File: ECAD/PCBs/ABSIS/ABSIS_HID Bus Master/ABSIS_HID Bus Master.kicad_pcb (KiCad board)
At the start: 2 copper layers, 90.8 x 53.3 mm, 19 parts, among them J1 PWR IN, J2 BUS #1, U0 ProMicro, U1 MAX487EESA+T

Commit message: Drawing Sheet & Silkscreen Update - ABSIS
On all ABSIS PCBs:

1:  Updated/Relinked Drawing Sheet for both PCB and Schematics
2:  Standardized Silkscreen (if required)
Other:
- board text added: "REV: 2"
- board text removed: "REV: 1"
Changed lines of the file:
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@@
   (paper "A4")
   (title_block
-    (title "ABSIS RS485 BUS MASTER")
-    (date "2020-11-04")
+    (title "ABSIS HID Bus Master")
+    (date "2023-02-10")
     (rev "2")
-    (company "OPENHORNET.COM")
-    (comment 1 "CC BY-NC-SA")
+    (company "www.openhornet.com")
+    (comment 1 "License:  CC BY-NC-SA")
   )
   (layers
@@
     (effects (font (size 1 1) (thickness 0.15)))
   )
-  (gr_text "REV: 1" (at 191.643 75.819) (layer "F.SilkS")
+  (gr_text "REV: 2" (at 191.643 75.819) (layer "F.SilkS")
     (effects (font (size 0.8 0.8) (thickness 0.15)))
   )

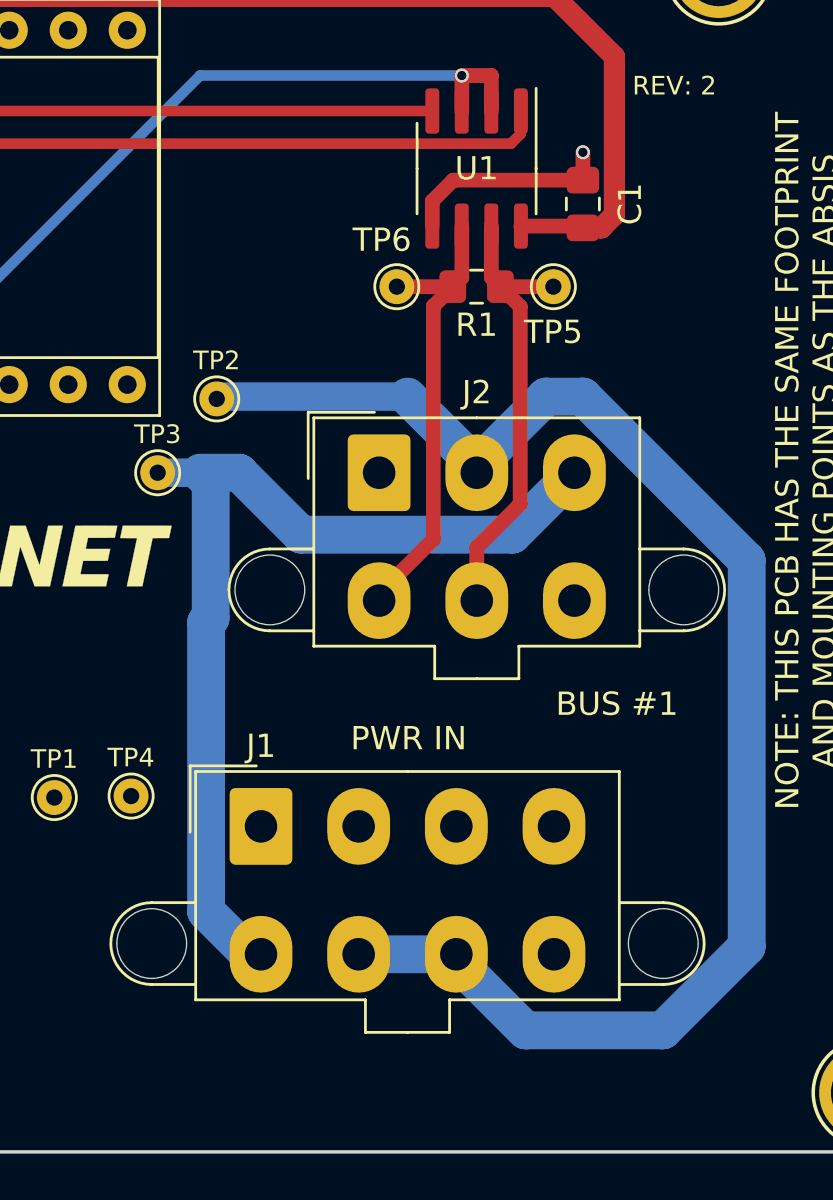
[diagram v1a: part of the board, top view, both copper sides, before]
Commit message: Review: ABSIS_HID Bus Master 100% Complete.
Updated Model and Footprint libraries
Updated PCB with correct footprint paths to point towards OH libraries
Updated production files
Added .PNGs and updated STEP file
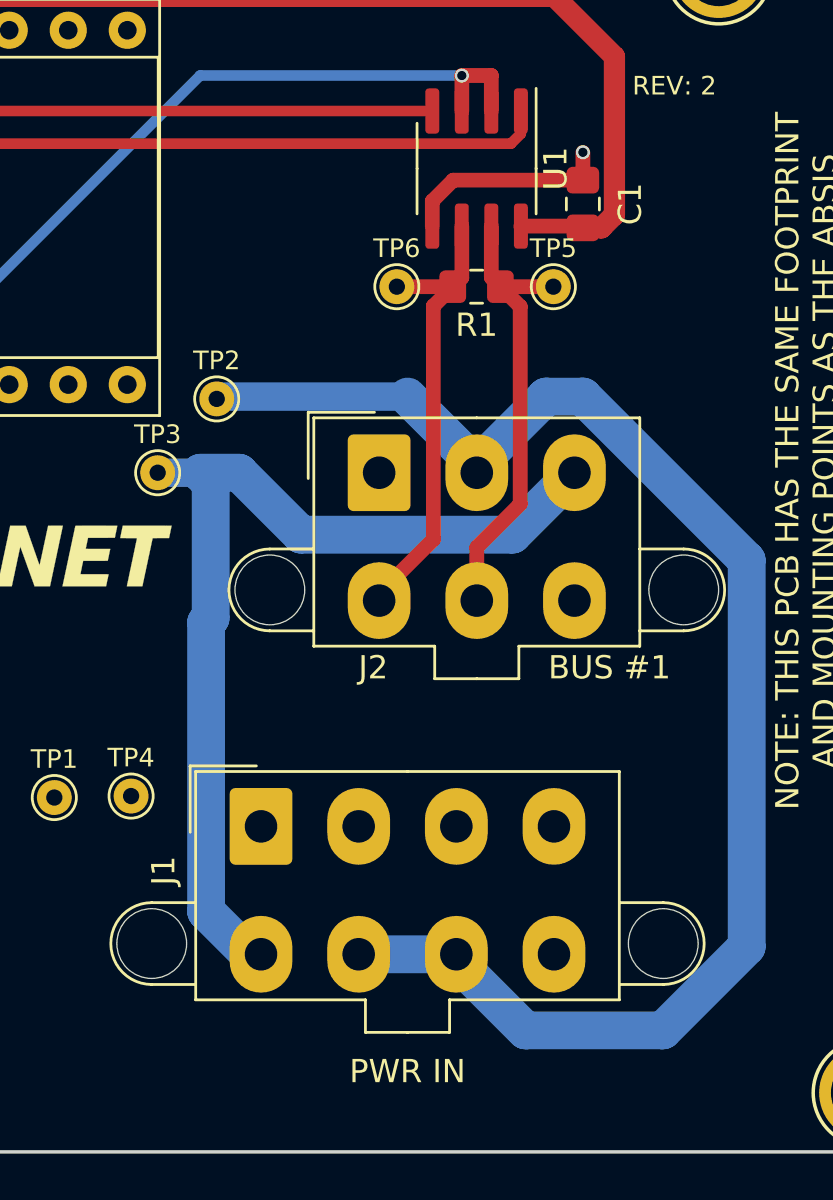
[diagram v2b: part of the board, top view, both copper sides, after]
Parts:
- C1: footprint Capacitor_SMD:C_0805_2012Metric_Pad1.15x1.40mm_HandSolder -> OH_Footprints:C_0805_2012Metric_Pad1.15x1.40mm_HandSolder
- J1: footprint Connector_Molex:Molex_Mini-Fit_Jr_5566-08A2_2x04_P4.20mm_Vertical -> OH_Footprints:Molex_Mini-Fit_Jr_5566-08A2_2x04_P4.20mm_Vertical
- J2: footprint Connector_Molex:Molex_Mini-Fit_Jr_5566-06A2_2x03_P4.20mm_Vertical -> OH_Footprints:Molex_Mini-Fit_Jr_5566-06A2_2x03_P4.20mm_Vertical
- LOGO1: footprint KiCAD Libraries:OH_LOGO_37.7mm_5.9mm -> OH_Footprints:OH_LOGO_37.7mm_5.9mm
- LOGO3: footprint KiCAD Libraries:CC-BY-NC-SA-Small -> OH_Footprints:CC-BY-NC-SA-Small
- LOGO4: footprint KiCAD Libraries:OH_LOGO_LARGE -> OH_Footprints:OH_LOGO_LARGE
- MK1, MK3, MK4, MK6: footprint Socket_Arduino_Mega:Arduino_1pin -> OH_Footprints:Arduino_1pin
- R1: footprint Resistor_SMD:R_0805_2012Metric_Pad1.15x1.40mm_HandSolder -> OH_Footprints:R_0805_2012Metric_Pad1.15x1.40mm_HandSolder
- TP1, TP2, TP3, TP4, TP5, TP6: footprint TestPoint:TestPoint_THTPad_D1.5mm_Drill0.7mm -> OH_Footprints:TestPoint_THTPad_D1.5mm_Drill0.7mm
- U0: footprint Package_DIP:DIP-24_W15.24mm_Socket -> OH_Footprints:DIP-24_W15.24mm_Socket
- U1: footprint Package_SO:SOIC-8_3.9x4.9mm_P1.27mm -> OH_Footprints:SOIC-8_3.9x4.9mm_P1.27mm

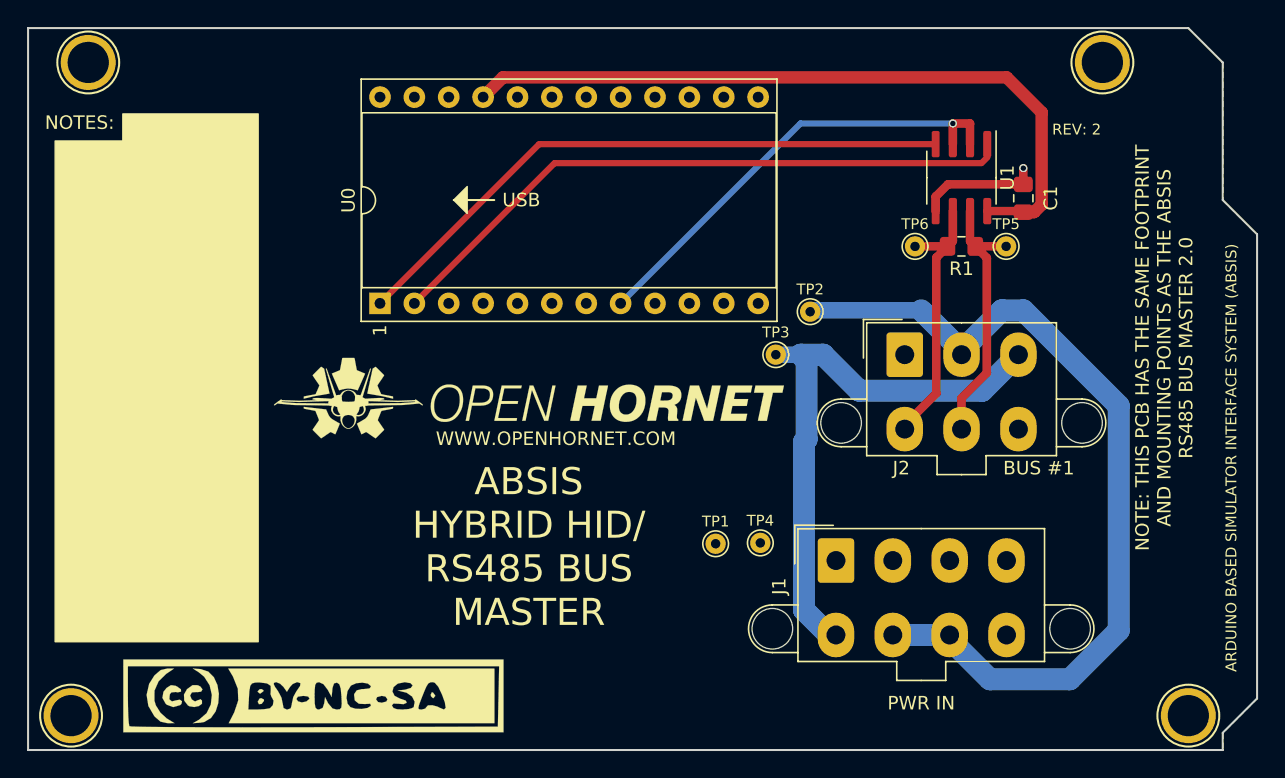
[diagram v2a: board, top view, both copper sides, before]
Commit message: KiCad 7 Transition - ABSIS_HID Bus Controller
ABSIS_Backlight Controller Schematic
-Adjusted orientation of text on a few symbols

Adjusted RAW pin on Pro Micro symbol from Power Output to Power Input.

Schematic & PCB standardization
- Updated symbol links
- Recompiled Assets and Manufacturing Files
- Updated LOGO symbols to schematic
- Recompiled Assets and Manufacturing Files (removed "TOP_BOM")
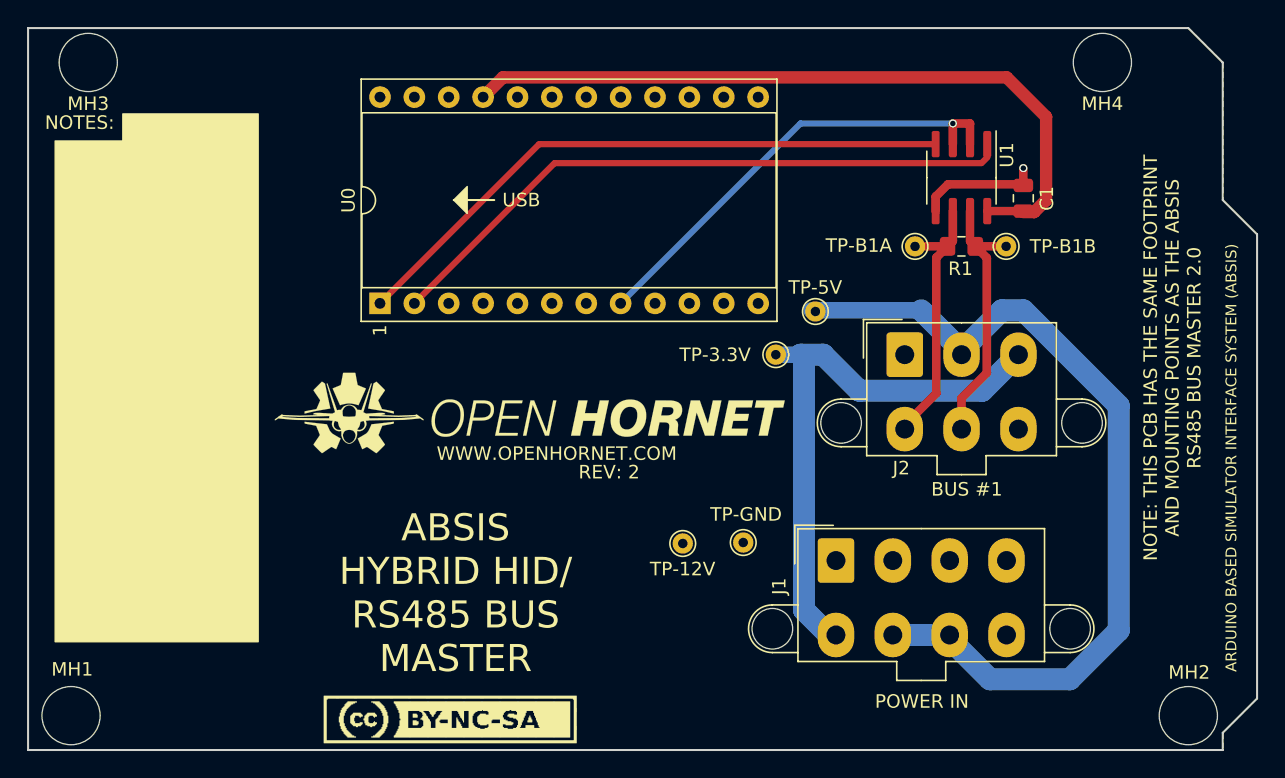
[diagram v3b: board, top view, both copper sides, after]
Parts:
- C1: footprint OH_Footprints:C_0805_2012Metric_Pad1.15x1.40mm_HandSolder -> OH_Footprints:C_0805_2012Metric
- J1: value PWR IN -> Molex_Mini-Fit_Jr._2x04
- J2: value BUS #1 -> Mini-Fit Jr. 2x03
- LOGO1: renamed from LOGO4; value OpenHornetLogoSmall -> LOGO; footprint OH_Footprints:OH_LOGO_LARGE -> OH_Footprints:LOGO_OH_NoText_Large
- LOGO2: renamed from LOGO1; value OpenHornetLogoSmall -> LOGO; footprint OH_Footprints:OH_LOGO_37.7mm_5.9mm -> OH_Footprints:LOGO_OH_Text_Small
- LOGO3: value OpenHornetLogoSmall -> LOGO; footprint OH_Footprints:CC-BY-NC-SA-Small -> OH_Footprints:LOGO_CC-BY-NC-SA_Half_Small
- MH1: renamed from MK1; value MH -> 6x32 / 4mm; footprint OH_Footprints:Arduino_1pin -> OH_Footprints:MountingHole_6-32_PHS
- MH2: renamed from MK3; value MH -> 6x32 / 4mm; footprint OH_Footprints:Arduino_1pin -> OH_Footprints:MountingHole_6-32_PHS
- MH3: renamed from MK4; value MH -> 6x32 / 4mm; footprint OH_Footprints:Arduino_1pin -> OH_Footprints:MountingHole_6-32_PHS
- MH4: renamed from MK6; value MH -> 6x32 / 4mm; footprint OH_Footprints:Arduino_1pin -> OH_Footprints:MountingHole_6-32_PHS
- TP1: value TP-12 -> TestPoint
- TP2: value TP-5V -> TestPoint
- TP3: value TP-3.3V -> TestPoint
- TP4: value TP-GND -> TestPoint
- TP5: value TP-B1B -> TestPoint
- TP6: value TP-B1A -> TestPoint
- U0: value ProMicro -> ProMicro_5V/16Hz
- moved TP1 2.43 mm to (162.5, 106.4)
- moved TP4 1.26 mm to (167.0, 106.3)
- moved LOGO2 1.10 mm to (151.2, 96.8)
- moved LOGO3 0.85 mm to (136.0, 117.7)
- moved TP2 0.39 mm to (172.3, 89.3)
- turned R1 to 0 degrees
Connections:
- R1 pad 1: /BUS1-B -> /BUS1-A
- R1 pad 2: /BUS1-A -> /BUS1-B
- U0 pad 10: Net-(U0-Pad10) -> unconnected-(U0-D7-Pad10)
- U0 pad 11: Net-(U0-Pad11) -> unconnected-(U0-D8/A8-Pad11)
- U0 pad 12: Net-(U0-Pad12) -> unconnected-(U0-~{D9/A9}-Pad12)
- U0 pad 13: Net-(U0-Pad13) -> unconnected-(U0-~{D10/A10}-Pad13)
- U0 pad 14: Net-(U0-Pad14) -> unconnected-(U0-D16/MOSI-Pad14)
- U0 pad 15: Net-(U0-Pad15) -> unconnected-(U0-D14/MISO-Pad15)
- U0 pad 16: Net-(U0-Pad16) -> unconnected-(U0-D15/SCK-Pad16)
- U0 pad 17: Net-(U0-Pad17) -> unconnected-(U0-A0-Pad17)
- U0 pad 18: Net-(U0-Pad18) -> unconnected-(U0-A1-Pad18)
- U0 pad 19: Net-(U0-Pad19) -> unconnected-(U0-A2-Pad19)
- U0 pad 20: Net-(U0-Pad20) -> unconnected-(U0-A3-Pad20)
- U0 pad 5: Net-(U0-Pad5) -> unconnected-(U0-SDA/D2-Pad5)
- U0 pad 6: Net-(U0-Pad6) -> unconnected-(U0-~{SCL/D3}-Pad6)
- U0 pad 7: Net-(U0-Pad7) -> unconnected-(U0-D4/A6-Pad7)
- U0 pad 9: Net-(U0-Pad9) -> unconnected-(U0-~{D6/A7}-Pad9)
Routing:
- net /+5V_SUPPLY: track 64.8 -> 64.1 mm
- net /+3.3V_SUPPLY: track 42.4 -> 41.7 mm
